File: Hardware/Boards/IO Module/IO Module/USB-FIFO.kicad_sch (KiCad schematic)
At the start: 26 parts, among them U13 FT600Q, Y2 30Mhz

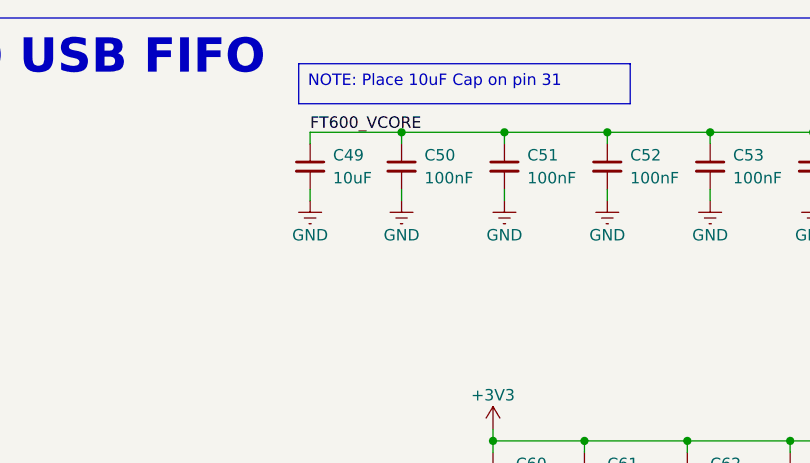
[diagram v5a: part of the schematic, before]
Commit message: Updated PCB routing for IO Module
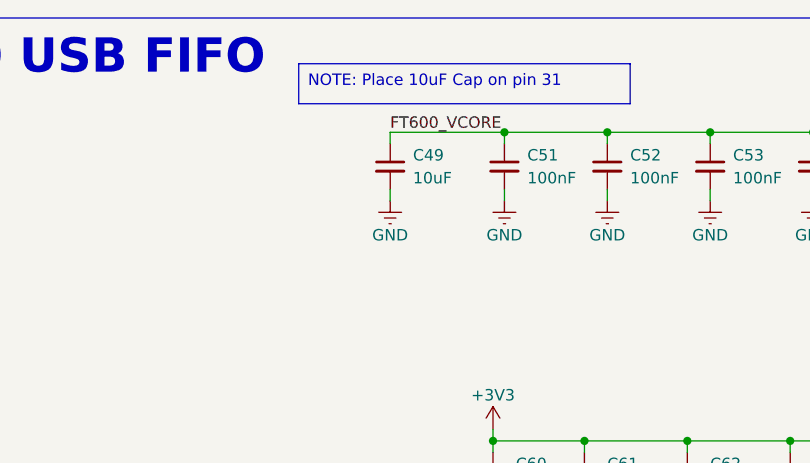
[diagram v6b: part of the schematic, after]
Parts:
- removed C50: 100nF, Capacitor_SMD:C_0402_1005Metric, symbol Device:C_Small
- C51, C52, C53, C54, C55, C56, C57, C58, C59, C60, C61, C62, C63, C64, C65, C66: footprint Capacitor_SMD:C_0402_1005Metric -> Capacitor_SMD:C_0201_0603Metric
- R103, R42, R43, R44, R45, R46: footprint Resistor_SMD:R_0402_1005Metric -> Resistor_SMD:R_0201_0603Metric
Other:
- moved on the sheet: C49
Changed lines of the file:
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@@
 	)
 	(junction
-		(at 146.05 67.31)
-		(diameter 0)
-		(color 0 0 0 0)
-	)
-	(junction
 		(at 215.9 77.47)
 		(diameter 0)
@@
 		)
 	)
-	(wire
-		(pts
-			(xy 135.89 67.31) (xy 146.05 67.31)
-		)
-		(stroke
-			(width 0)
-			(type default)
-		)
-	)
 	(bus
 		(pts
@@
 	(wire
 		(pts
-			(xy 146.05 73.66) (xy 146.05 74.93)
-		)
-		(stroke
-			(width 0)
-			(type default)
-		)
-	)
-	(wire
-		(pts
 			(xy 266.7 73.66) (xy 266.7 74.93)
 		)
@@
 	(wire
 		(pts
-			(xy 146.05 67.31) (xy 157.48 67.31)
+			(xy 144.78 67.31) (xy 157.48 67.31)
 		)
 		(stroke
@@
 	(wire
 		(pts
-			(xy 146.05 68.58) (xy 146.05 67.31)
-		)
-		(stroke
-			(width 0)
-			(type default)
-		)
-	)
-	(wire
-		(pts
 			(xy 187.96 132.08) (xy 187.96 130.81)
 		)
@@
 	(wire
 		(pts
-			(xy 135.89 73.66) (xy 135.89 74.93)
+			(xy 144.78 73.66) (xy 144.78 74.93)
 		)
 		(stroke
@@
 	(wire
 		(pts
-			(xy 135.89 68.58) (xy 135.89 67.31)
+			(xy 144.78 68.58) (xy 144.78 67.31)
 		)
 		(stroke
@@
 	)
 	(label "FT600_VCORE"
-		(at 135.89 67.31 0)
+		(at 144.78 67.31 0)
 		(fields_autoplaced yes)
 		(effects
@@
 			)
 		)
-		(property "Footprint" "Resistor_SMD:R_0402_1005Metric"
+		(property "Footprint" "Resistor_SMD:R_0201_0603Metric"
 			(at 178.054 133.096 90)
 			(effects
@@
 			)
 		)
-		(property "Footprint" "Capacitor_SMD:C_0402_1005Metric"
+		(property "Footprint" "Capacitor_SMD:C_0201_0603Metric"
 			(at 191.77 71.12 0)
 			(effects
@@
 			)
 		)
-		(property "Footprint" "Capacitor_SMD:C_0402_1005Metric"
+		(property "Footprint" "Capacitor_SMD:C_0201_0603Metric"
 			(at 278.13 71.12 0)
 			(effects
@@
 			)
 		)
-		(property "Footprint" "Capacitor_SMD:C_0402_1005Metric"
+		(property "Footprint" "Capacitor_SMD:C_0201_0603Metric"
 			(at 168.91 71.12 0)
 			(effects
@@
 			)
 		)
-		(property "Footprint" "Capacitor_SMD:C_0402_1005Metric"
+		(property "Footprint" "Capacitor_SMD:C_0201_0603Metric"
 			(at 177.8 105.41 0)
 			(effects
@@
 			)
 		)
-		(property "Footprint" "Capacitor_SMD:C_0402_1005Metric"
+		(property "Footprint" "Capacitor_SMD:C_0201_0603Metric"
 			(at 200.66 105.41 0)
 			(effects
@@
 			)
 		)
-		(property "Footprint" "Capacitor_SMD:C_0402_1005Metric"
+		(property "Footprint" "Capacitor_SMD:C_0201_0603Metric"
 			(at 156.21 105.41 0)
 			(effects
@@
 	(symbol
 		(lib_id "power:GND")
-		(at 135.89 74.93 0)
+		(at 144.78 74.93 0)
 		(unit 1)
 		(exclude_from_sim no)
@@
 		(dnp no)
 		(property "Reference" "#PWR0115"
-			(at 135.89 78.74 0)
+			(at 144.78 78.74 0)
 			(effects
 				(font
@@
 		)
 		(property "Value" "GND"
-			(at 135.89 78.74 0)
+			(at 144.78 78.74 0)
 			(effects
 				(font
@@
 		)
 		(property "Footprint" ""
-			(at 135.89 74.93 0)
+			(at 144.78 74.93 0)
 			(effects
 				(font
@@
 		)
 		(property "Datasheet" ""
-			(at 135.89 74.93 0)
+			(at 144.78 74.93 0)
 			(effects
 				(font
@@
 		)
 		(property "Description" "Power symbol creates a global label with name \"GND\" , ground"
-			(at 135.89 74.93 0)
+			(at 144.78 74.93 0)
 			(effects
 				(font
@@
 			)
 		)
-		(property "Footprint" "Capacitor_SMD:C_0402_1005Metric"
+		(property "Footprint" "Capacitor_SMD:C_0201_0603Metric"
 			(at 187.96 171.45 0)
 			(effects
@@
 			)
 		)
-		(property "Footprint" "Capacitor_SMD:C_0402_1005Metric"
+		(property "Footprint" "Capacitor_SMD:C_0201_0603Metric"
 			(at 255.27 71.12 0)
 			(effects
@@
 			)
 		)
-		(property "Footprint" "Resistor_SMD:R_0402_1005Metric"
+		(property "Footprint" "Resistor_SMD:R_0201_0603Metric"
 			(at 112.014 124.206 90)
 			(effects
@@
 	(symbol
 		(lib_id "Device:C_Small")
-		(at 135.89 71.12 0)
+		(at 144.78 71.12 0)
 		(unit 1)
 		(exclude_from_sim no)
@@
 		(fields_autoplaced yes)
 		(property "Reference" "C49"
-			(at 138.43 69.8562 0)
+			(at 147.32 69.8562 0)
 			(effects
 				(font
@@
 		)
 		(property "Value" "10uF"
-			(at 138.43 72.3962 0)
+			(at 147.32 72.3962 0)
 			(effects
 				(font
@@
 		)
 		(property "Footprint" "Capacitor_SMD:C_0603_1608Metric"
-			(at 135.89 71.12 0)
+			(at 144.78 71.12 0)
 			(effects
 				(font
@@
 		)
 		(property "Datasheet" "~"
-			(at 135.89 71.12 0)
+			(at 144.78 71.12 0)
 			(effects
 				(font
@@
 		)
 		(property "Description" "Unpolarized capacitor, small symbol"
-			(at 135.89 71.12 0)
+			(at 144.78 71.12 0)
 			(effects
 				(font
@@
 			)
 		)
-		(property "Footprint" "Resistor_SMD:R_0402_1005Metric"
+		(property "Footprint" "Resistor_SMD:R_0201_0603Metric"
 			(at 186.944 126.746 90)
 			(effects
@@
 	(symbol
 		(lib_id "power:GND")
-		(at 146.05 74.93 0)
-		(unit 1)
-		(exclude_from_sim no)
-		(in_bom yes)
-		(on_board yes)
-		(dnp no)
-		(property "Reference" "#PWR0116"
-			(at 146.05 78.74 0)
-			(effects
-				(font
-					(size 1.27 1.27)
-				)
-				(hide yes)
-			)
-		)
-		(property "Value" "GND"
-			(at 146.05 78.74 0)
-			(effects
-				(font
-					(size 1.27 1.27)
-				)
-			)
-		)
-		(property "Footprint" ""
-			(at 146.05 74.93 0)
-			(effects
-				(font
-					(size 1.27 1.27)
-				)
-				(hide yes)
-			)
-		)
-		(property "Datasheet" ""
-			(at 146.05 74.93 0)
-			(effects
-				(font
-					(size 1.27 1.27)
-				)
-				(hide yes)
-			)
-		)
-		(property "Description" "Power symbol creates a global label with name \"GND\" , ground"
-			(at 146.05 74.93 0)
-			(effects
-				(font
-					(size 1.27 1.27)
-				)
-				(hide yes)
-			)
-		)
-		(pin "1"
-		)
-		(instances
-			(project "IO Module"
-				(path "/884396b6-238b-495e-b731-e47ad2523f76/dcc99803-8acd-4632-9c0b-7f677477cf65/0caf3050-48d7-4c2b-bd75-8084d37ef6b3"
-					(reference "#PWR0116")
-					(unit 1)
-				)
-			)
-		)
-	)
-	(symbol
-		(lib_id "power:GND")
 		(at 288.29 74.93 0)
 		(mirror y)
@@
 			)
 		)
-		(property "Footprint" "Capacitor_SMD:C_0402_1005Metric"
+		(property "Footprint" "Capacitor_SMD:C_0201_0603Metric"
 			(at 166.37 105.41 0)
 			(effects
@@
 			)
 		)
-		(property "Footprint" "Capacitor_SMD:C_0402_1005Metric"
+		(property "Footprint" "Capacitor_SMD:C_0201_0603Metric"
 			(at 158.75 171.45 0)
 			(effects
@@
 			)
 		)
-		(property "Footprint" "Capacitor_SMD:C_0402_1005Metric"
+		(property "Footprint" "Capacitor_SMD:C_0201_0603Metric"
 			(at 180.34 71.12 0)
 			(effects
@@
 	(symbol
 		(lib_id "Device:C_Small")
-		(at 146.05 71.12 0)
-		(unit 1)
-		(exclude_from_sim no)
-		(in_bom yes)
-		(on_board yes)
-		(dnp no)
-		(fields_autoplaced yes)
-		(property "Reference" "C50"
-			(at 148.59 69.8562 0)
-			(effects
-				(font
-					(size 1.27 1.27)
-				)
-				(justify left)
-			)
-		)
-		(property "Value" "100nF"
-			(at 148.59 72.3962 0)
-			(effects
-				(font
-					(size 1.27 1.27)
-				)
-				(justify left)
-			)
-		)
-		(property "Footprint" "Capacitor_SMD:C_0402_1005Metric"
-			(at 146.05 71.12 0)
-			(effects
-				(font
-					(size 1.27 1.27)
-				)
-				(hide yes)
-			)
-		)
-		(property "Datasheet" "~"
-			(at 146.05 71.12 0)
-			(effects
-				(font
-					(size 1.27 1.27)
-				)
-				(hide yes)
-			)
-		)
-		(property "Description" "Unpolarized capacitor, small symbol"
-			(at 146.05 71.12 0)
-			(effects
-				(font
-					(size 1.27 1.27)
-				)
-				(hide yes)
-			)
-		)
-		(pin "1"
-		)
-		(pin "2"
-		)
-		(instances
-			(project "IO Module"
-				(path "/884396b6-238b-495e-b731-e47ad2523f76/dcc99803-8acd-4632-9c0b-7f677477cf65/0caf3050-48d7-4c2b-bd75-8084d37ef6b3"
-					(reference "C50")
-					(unit 1)
-				)
-			)
-		)
-	)
-	(symbol
-		(lib_id "Device:C_Small")
 		(at 203.2 71.12 0)
 		(unit 1)
@@
 			)
 		)
-		(property "Footprint" "Capacitor_SMD:C_0402_1005Metric"
+		(property "Footprint" "Capacitor_SMD:C_0201_0603Metric"
 			(at 203.2 71.12 0)
 			(effects
@@
 			)
 		)
-		(property "Footprint" "Resistor_SMD:R_0402_1005Metric"
+		(property "Footprint" "Resistor_SMD:R_0201_0603Metric"
 			(at 112.014 134.366 90)
 			(effects
@@
 			)
 		)
-		(property "Footprint" "Capacitor_SMD:C_0402_1005Metric"
+		(property "Footprint" "Capacitor_SMD:C_0201_0603Metric"
 			(at 266.7 71.12 0)
 			(effects
@@
 			)
 		)
-		(property "Footprint" "Capacitor_SMD:C_0402_1005Metric"
+		(property "Footprint" "Capacitor_SMD:C_0201_0603Metric"
 			(at 189.23 105.41 0)
 			(effects
@@
 			)
 		)
-		(property "Footprint" "Resistor_SMD:R_0402_1005Metric"
+		(property "Footprint" "Resistor_SMD:R_0201_0603Metric"
 			(at 148.844 138.176 90)
 			(effects
@@
 			)
 		)
-		(property "Footprint" "Resistor_SMD:R_0402_1005Metric"
+		(property "Footprint" "Resistor_SMD:R_0201_0603Metric"
 			(at 209.296 155.956 90)
 			(effects
@@
 			)
 		)
-		(property "Footprint" "Capacitor_SMD:C_0402_1005Metric"
+		(property "Footprint" "Capacitor_SMD:C_0201_0603Metric"
 			(at 157.48 71.12 0)
 			(effects
@@
 			)
 		)
-		(property "Footprint" "Capacitor_SMD:C_0402_1005Metric"
+		(property "Footprint" "Capacitor_SMD:C_0201_0603Metric"
 			(at 288.29 71.12 0)
 			(effects
